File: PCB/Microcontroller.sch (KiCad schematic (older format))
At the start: 0 parts

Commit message: Add microcontroller/radio module to library
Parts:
- added U?: BMD-360, Parts:BMD-360, symbol Parts:BMD-360
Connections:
- new net: U?.1 (GND), U?.16 (GND), U?.18 (GND), U?.2 (GND), U?.29 (GND), U?.3 (GND), U?.30 (GND), U?.4 (GND), U?.45 (GND), U?.46 (GND), U?.47 (GND), U?.5 (GND)
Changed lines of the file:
@@
 Comment4 ""
 $EndDescr
+$Comp
+L Parts:BMD-360 U?
+U 1 1 5DCF155F
+P 5200 3300
+F 0 "U?" H 5200 4465 50  0000 C CNN
+F 1 "BMD-360" H 5200 4374 50  0000 C CNN
+F 2 "Parts:BMD-360" H 5200 2100 50  0001 C BNN
+F 3 "https://www.u-blox.com/en/product/bmd-360-open-cpu" H 5300 2000 50  0001 L BNN
+	1    5200 3300
+	1    0    0    -1
+$EndComp
 $EndSCHEMATC

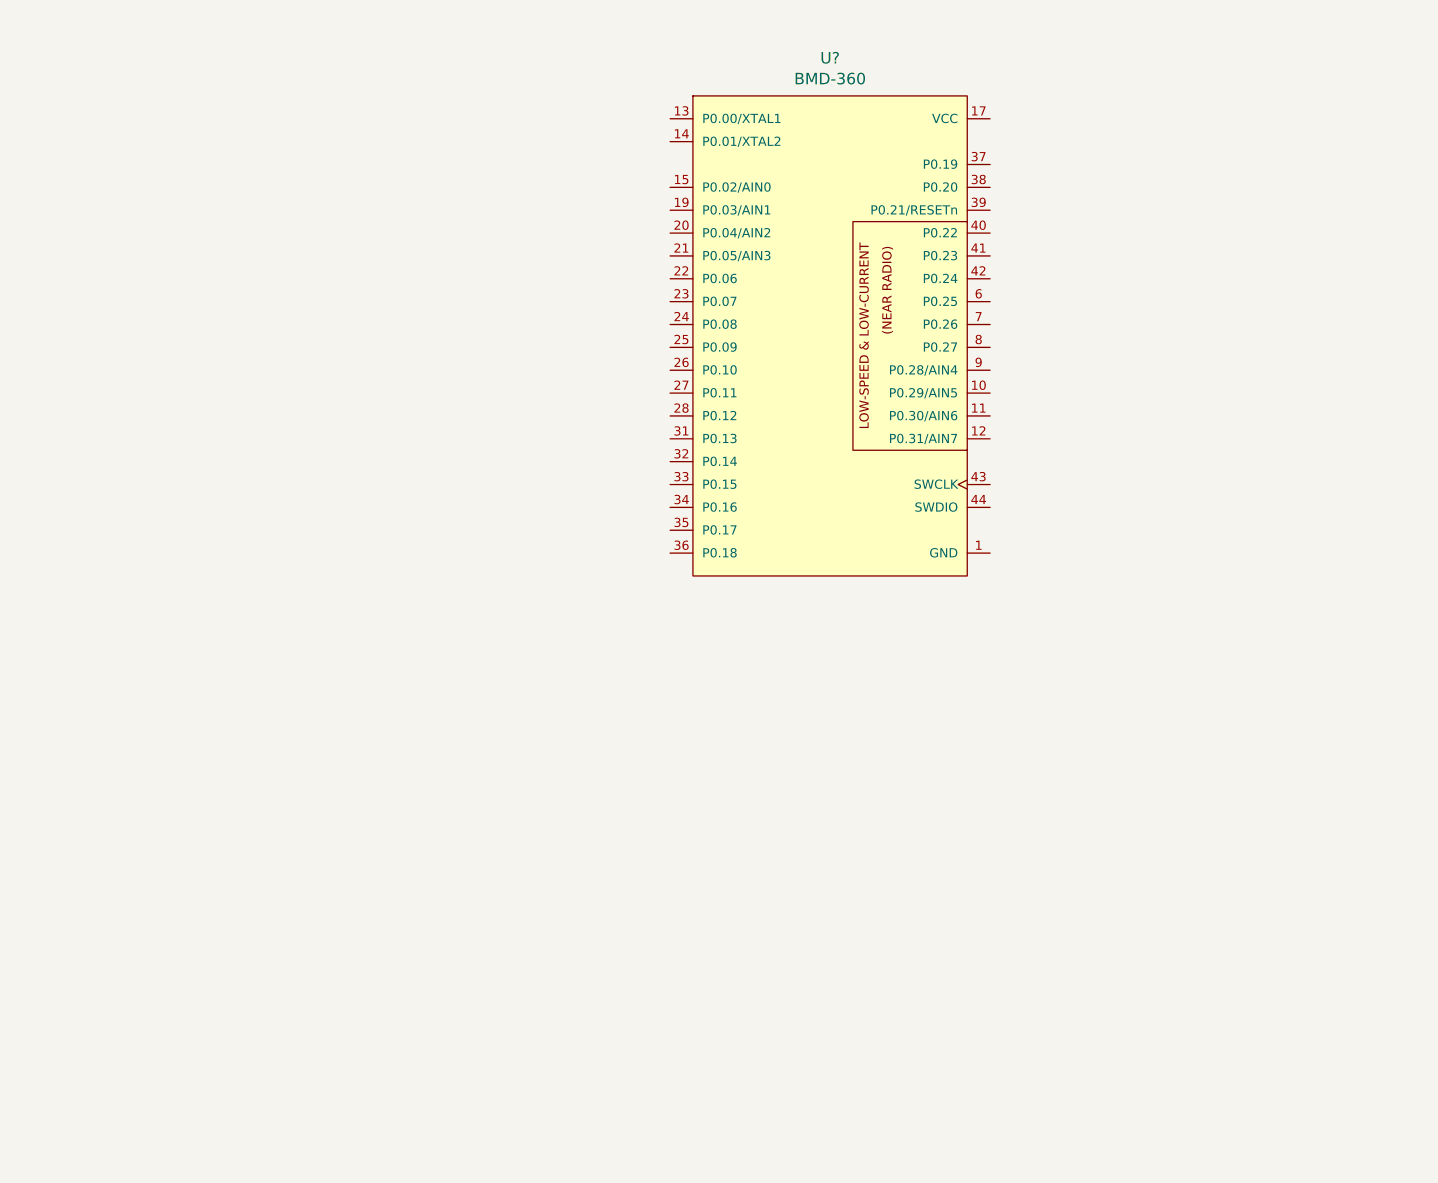
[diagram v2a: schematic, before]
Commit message: Cleanup FPGA ground pins in library, begin adding components to schematic
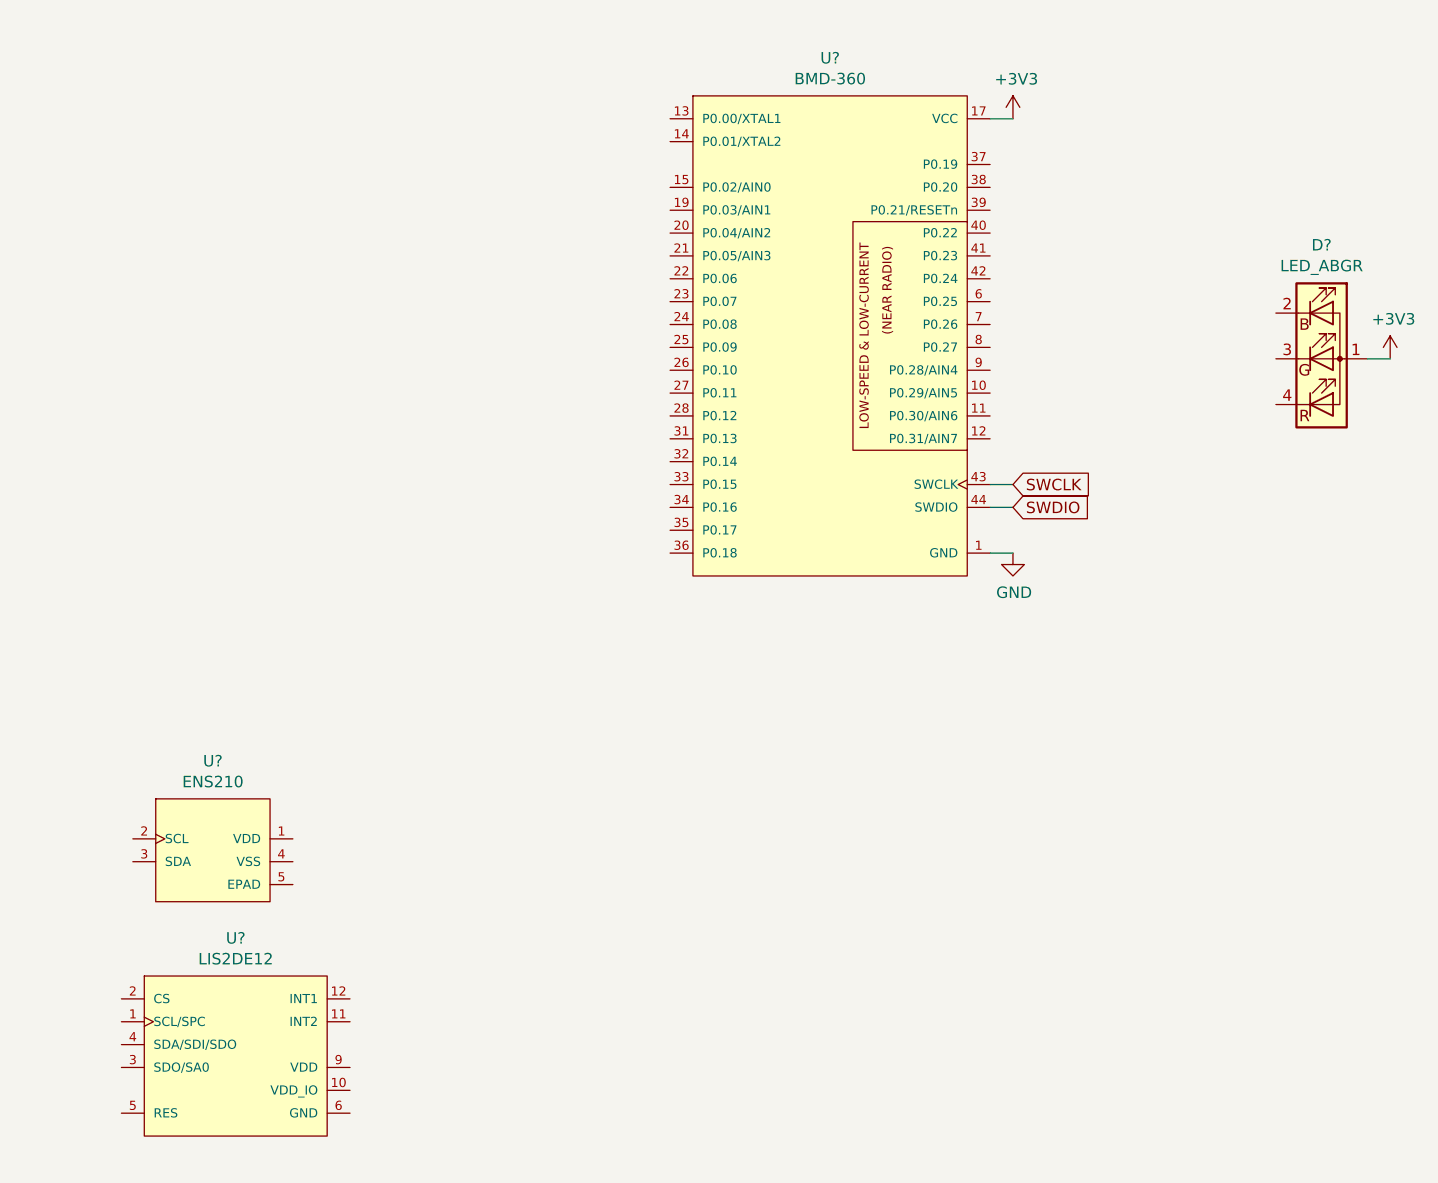
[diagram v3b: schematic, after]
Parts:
- added D?: LED_ABGR, Parts:CLMVC-FKA, symbol Parts:LED_ABGR
- added U?: ENS210, Parts:QFN4-PAD, symbol Parts:ENS210
- added U?: LIS2DE12, Parts:LGA12, symbol Parts:LIS2DE12
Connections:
- net GND: now reaches U?.1 (GND), U?.16 (GND), U?.18 (GND), U?.2 (GND), U?.29 (GND), U?.3 (GND), U?.30 (GND), U?.4 (GND), U?.45 (GND), U?.46 (GND), U?.47 (GND), U?.5 (GND)
- net +3V3: now reaches U?.17 (VCC)
- net +3V3: now also D?.1 (A)
- net SWCLK: now reaches U?.43 (SWCLK)
- net SWDIO: now reaches U?.44 (SWDIO)
- new net: U?.6 (GND), U?.7 (GND), U?.8 (GND)
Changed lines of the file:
@@
+	1    0    0    -1
+$EndComp
+$Comp
+L Parts:LED_ABGR D?
+U 1 1 5DCF3816
+P 7350 3450
+F 0 "D?" H 7350 3947 50  0000 C CNN
+F 1 "LED_ABGR" H 7350 3856 50  0000 C CNN
+F 2 "Parts:CLMVC-FKA" H 7350 3025 50  0001 C CNN
+F 3 "https://www.cree.com/led-components/media/documents/1273-CLMVC-FKA.pdf" H 7350 3400 50  0001 C CNN
+	1    7350 3450
+	1    0    0    -1
+$EndComp
+$Comp
+L power:+3V3 #PWR?
+U 1 1 5DCF44EC
+P 6000 2400
+F 0 "#PWR?" H 6000 2250 50  0001 C CNN
+F 1 "+3V3" H 6015 2573 50  0000 C CNN
+F 2 "" H 6000 2400 50  0001 C CNN
+F 3 "" H 6000 2400 50  0001 C CNN
+	1    6000 2400
+	1    0    0    -1
+$EndComp
+Wire Wire Line
+	5900 2400 6000 2400
+$Comp
+L power:GND #PWR?
+U 1 1 5DCF5A78
+P 6000 4300
+F 0 "#PWR?" H 6000 4050 50  0001 C CNN
+F 1 "GND" H 6005 4127 50  0000 C CNN
+F 2 "" H 6000 4300 50  0001 C CNN
+F 3 "" H 6000 4300 50  0001 C CNN
+	1    6000 4300
+	1    0    0    -1
+$EndComp
+Wire Wire Line
+	5900 4300 6000 4300
+Text GLabel 6000 4000 2    50   Input ~ 0
+SWCLK
+Text GLabel 6000 4100 2    50   Input ~ 0
+SWDIO
+Wire Wire Line
+	5900 4000 6000 4000
+Wire Wire Line
+	6000 4100 5900 4100
+$Comp
+L power:+3V3 #PWR?
+U 1 1 5DCF6F82
+P 7650 3450
+F 0 "#PWR?" H 7650 3300 50  0001 C CNN
+F 1 "+3V3" H 7665 3623 50  0000 C CNN
+F 2 "" H 7650 3450 50  0001 C CNN
+F 3 "" H 7650 3450 50  0001 C CNN
+	1    7650 3450
+	1    0    0    -1
+$EndComp
+Wire Wire Line
+	7550 3450 7650 3450
+$Comp
+L Parts:ENS210 U?
+U 1 1 5DD2033C
+P 2500 5600
+F 0 "U?" H 2500 5990 50  0000 C CNN
+F 1 "ENS210" H 2500 5899 50  0000 C CNN
+F 2 "Parts:QFN4-PAD" H 2250 5300 50  0001 L BNN
+F 3 "https://ams.com/ens210" H 2450 4950 50  0001 L BNN
+	1    2500 5600
+	1    0    0    -1
+$EndComp
+$Comp
+L Parts:LIS2DE12 U?
+U 1 1 5DD21338
+P 2600 6550
+F 0 "U?" H 2600 7115 50  0000 C CNN
+F 1 "LIS2DE12" H 2600 7024 50  0000 C CNN
+F 2 "Parts:LGA12" H 2875 6975 50  0001 L BNN
+F 3 "https://www.st.com/content/st_com/en/products/mems-and-sensors/accelerometers/lis2de12.html" H 1800 7700 50  0001 L BNN
+	1    2600 6550
 	1    0    0    -1
 $EndComp

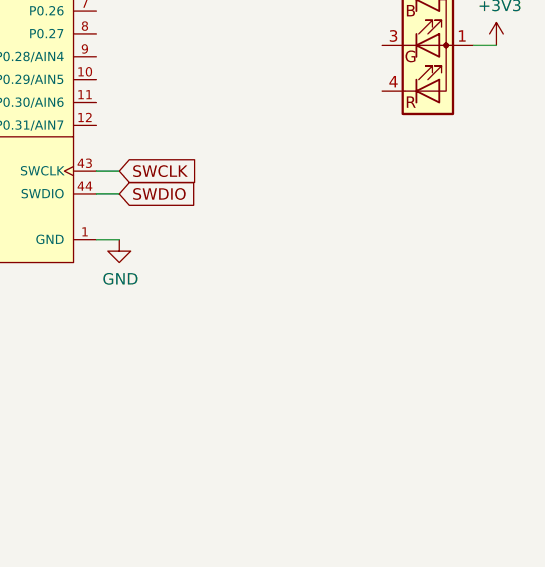
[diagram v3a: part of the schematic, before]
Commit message: Add push button to library
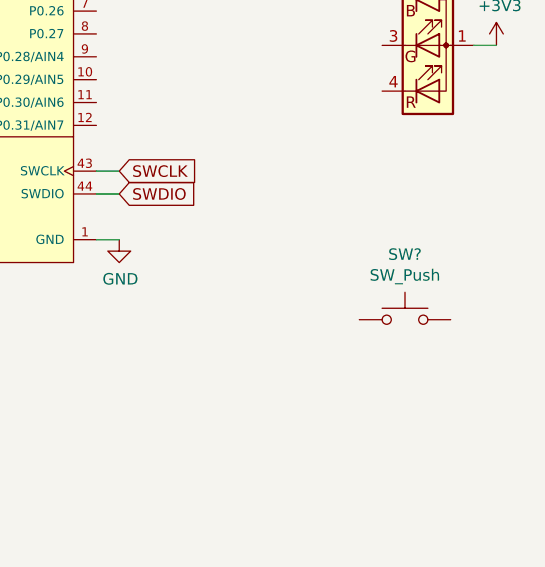
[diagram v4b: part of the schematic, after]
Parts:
- added SW?: SW_Push, Parts:PTS645SK43SM, symbol Switch:SW_Push
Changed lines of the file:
@@
+	1    0    0    -1
+$EndComp
+$Comp
+L Switch:SW_Push SW?
+U 1 1 5DCE5B76
+P 7250 4650
+F 0 "SW?" H 7250 4935 50  0000 C CNN
+F 1 "SW_Push" H 7250 4844 50  0000 C CNN
+F 2 "Parts:PTS645SK43SM" H 7250 4850 50  0001 C CNN
+F 3 "https://www.ckswitches.com/products/tactile/PTS645/" H 7250 4850 50  0001 C CNN
+	1    7250 4650
 	1    0    0    -1
 $EndComp

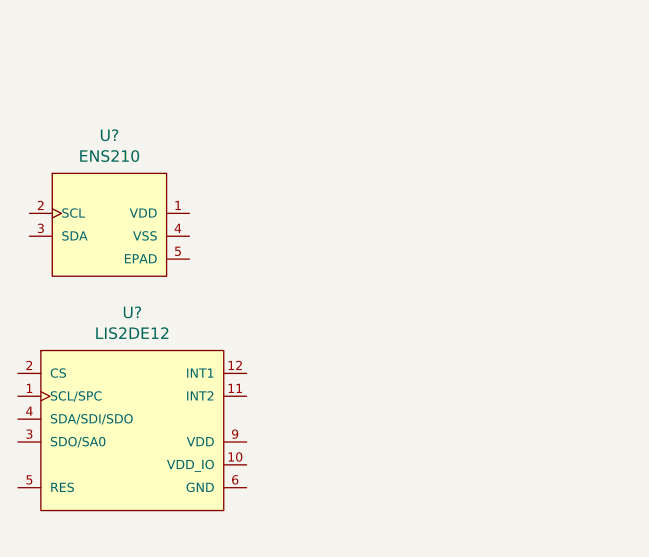
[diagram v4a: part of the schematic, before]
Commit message: Added "near radio" warning to microcontroller pins, connected more ICs to power rails, added transducer capacitive coupling
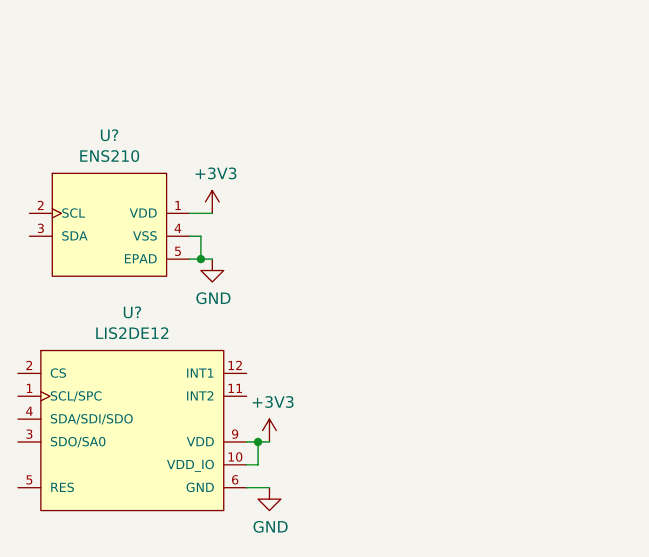
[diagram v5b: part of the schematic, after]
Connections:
- net +3V3: now also U?.1 (VDD), U?.10 (VDD_IO), U?.9 (VDD)
- net GND: now also U?.4 (VSS), U?.5 (EPAD), U?.6 (GND), U?.7 (GND), U?.8 (GND)
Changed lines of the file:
@@
 $EndComp
 $Comp
-L power:+3V3 #PWR?
+L power:+3V3 #PWR0125
 U 1 1 5DCF44EC
 P 6000 2400
-F 0 "#PWR?" H 6000 2250 50  0001 C CNN
+F 0 "#PWR0125" H 6000 2250 50  0001 C CNN
 F 1 "+3V3" H 6015 2573 50  0000 C CNN
 F 2 "" H 6000 2400 50  0001 C CNN
@@
 	5900 2400 6000 2400
 $Comp
-L power:GND #PWR?
+L power:GND #PWR0126
 U 1 1 5DCF5A78
 P 6000 4300
-F 0 "#PWR?" H 6000 4050 50  0001 C CNN
+F 0 "#PWR0126" H 6000 4050 50  0001 C CNN
 F 1 "GND" H 6005 4127 50  0000 C CNN
 F 2 "" H 6000 4300 50  0001 C CNN
@@
 	6000 4100 5900 4100
 $Comp
-L power:+3V3 #PWR?
+L power:+3V3 #PWR0127
 U 1 1 5DCF6F82
 P 7650 3450
-F 0 "#PWR?" H 7650 3300 50  0001 C CNN
+F 0 "#PWR0127" H 7650 3300 50  0001 C CNN
 F 1 "+3V3" H 7665 3623 50  0000 C CNN
 F 2 "" H 7650 3450 50  0001 C CNN
@@
 	1    0    0    -1
 $EndComp
+$Comp
+L power:+3V3 #PWR?
+U 1 1 5DE86491
+P 2950 5550
+F 0 "#PWR?" H 2950 5400 50  0001 C CNN
+F 1 "+3V3" H 2965 5723 50  0000 C CNN
+F 2 "" H 2950 5550 50  0001 C CNN
+F 3 "" H 2950 5550 50  0001 C CNN
+	1    2950 5550
+	1    0    0    -1
+$EndComp
+Wire Wire Line
+	2850 5550 2950 5550
+$Comp
+L power:GND #PWR?
+U 1 1 5DE86F13
+P 2950 5750
+F 0 "#PWR?" H 2950 5500 50  0001 C CNN
+F 1 "GND" H 2955 5577 50  0000 C CNN
+F 2 "" H 2950 5750 50  0001 C CNN
+F 3 "" H 2950 5750 50  0001 C CNN
+	1    2950 5750
+	1    0    0    -1
+$EndComp
+Wire Wire Line
+	2850 5650 2900 5650
+Wire Wire Line
+	2900 5650 2900 5750
+Wire Wire Line
+	2850 5750 2900 5750
+Connection ~ 2900 5750
+Wire Wire Line
+	2900 5750 2950 5750
+$Comp
+L power:+3V3 #PWR?
+U 1 1 5DE87DD2
+P 3200 6550
+F 0 "#PWR?" H 3200 6400 50  0001 C CNN
+F 1 "+3V3" H 3215 6723 50  0000 C CNN
+F 2 "" H 3200 6550 50  0001 C CNN
+F 3 "" H 3200 6550 50  0001 C CNN
+	1    3200 6550
+	1    0    0    -1
+$EndComp
+Wire Wire Line
+	3100 6550 3150 6550
+$Comp
+L power:GND #PWR?
+U 1 1 5DE88898
+P 3200 6750
+F 0 "#PWR?" H 3200 6500 50  0001 C CNN
+F 1 "GND" H 3205 6577 50  0000 C CNN
+F 2 "" H 3200 6750 50  0001 C CNN
+F 3 "" H 3200 6750 50  0001 C CNN
+	1    3200 6750
+	1    0    0    -1
+$EndComp
+Wire Wire Line
+	3150 6550 3150 6650
+Wire Wire Line
+	3150 6650 3100 6650
+Connection ~ 3150 6550
+Wire Wire Line
+	3150 6550 3200 6550
+Wire Wire Line
+	3100 6750 3200 6750
 $EndSCHEMATC

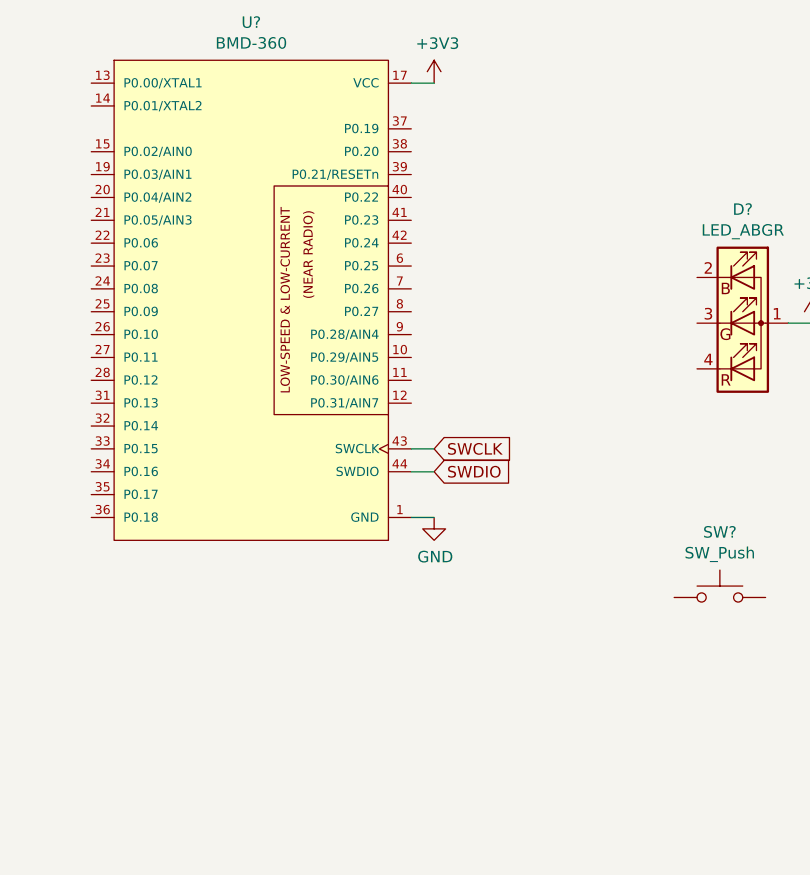
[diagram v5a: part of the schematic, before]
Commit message: Add debug headers for FPGA and microcontroller
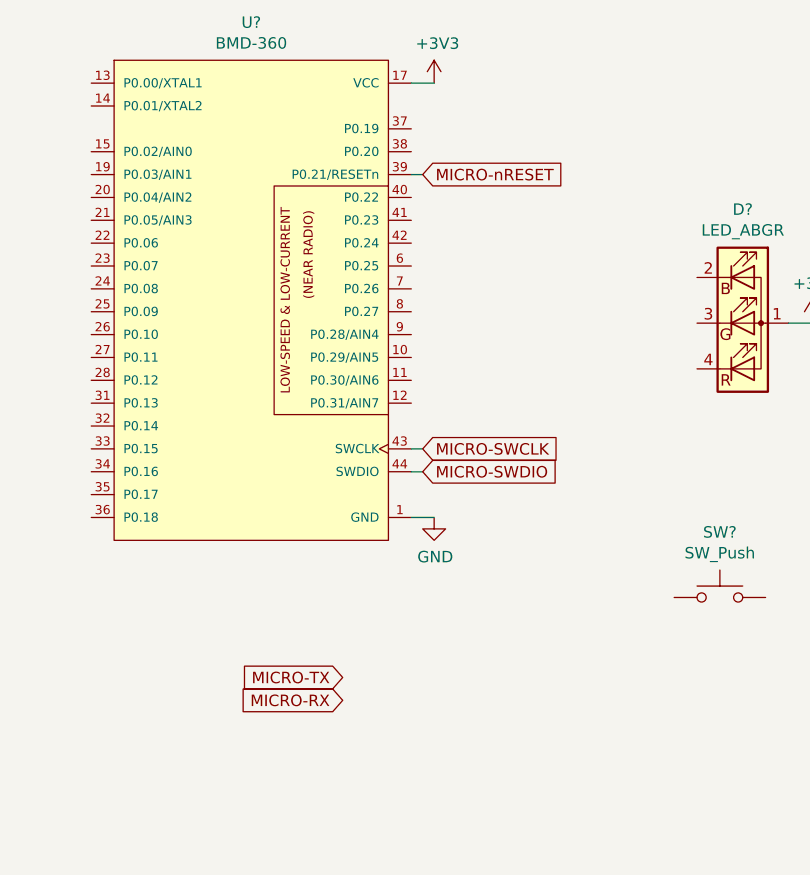
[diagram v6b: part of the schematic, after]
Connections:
- net MICRO-nRESET: now reaches U?.39 (P0.21/RESETn)
- net SWCLK renamed MICRO-SWCLK
- net SWDIO renamed MICRO-SWDIO
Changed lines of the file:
@@
 Wire Wire Line
 	5900 4300 6000 4300
-Text GLabel 6000 4000 2    50   Input ~ 0
-SWCLK
-Text GLabel 6000 4100 2    50   Input ~ 0
-SWDIO
+Text GLabel 5950 4000 2    50   Input ~ 0
+MICRO-SWCLK
+Text GLabel 5950 4100 2    50   Input ~ 0
+MICRO-SWDIO
 Wire Wire Line
-	5900 4000 6000 4000
+	5900 4000 5950 4000
 Wire Wire Line
-	6000 4100 5900 4100
+	5950 4100 5900 4100
 $Comp
 L power:+3V3 #PWR0127
@@
 Wire Wire Line
 	3100 6750 3200 6750
+Text GLabel 5600 5000 0    50   Input ~ 0
+MICRO-TX
+Text GLabel 5600 5100 0    50   Input ~ 0
+MICRO-RX
+Text GLabel 5950 2800 2    50   Input ~ 0
+MICRO-nRESET
+Wire Wire Line
+	5950 2800 5900 2800
 $EndSCHEMATC
